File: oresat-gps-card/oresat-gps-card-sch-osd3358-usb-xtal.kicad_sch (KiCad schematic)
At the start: 42 parts, among them U1 OSD3358-512M-BSM, U11 RCLAMP0504FB, Y1 24MHz, Y2 Crystal

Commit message: Routine Push
Various small changes made
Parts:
- removed TP104, TP137, TP138, TP139, TP165, TP166, TP167, TP168, TP169, TP170, TP171, TP172, TP173, TP174, TP59, TP60, TP69, TP70, TP71, TP72: 0.03x0.04, oresat-misc:TestPoint_Pad_D1.0mm, symbol oresat-misc:Test-Point-1mm-round
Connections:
- no-connect marks 1 -> 15

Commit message: Routine Push
First attempt to clean up schematic
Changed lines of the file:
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@@
 		)
 	)
-	(global_label "USB_CLI_P"
+	(hierarchical_label "USB_CLI_N"
 		(shape input)
-		(at 119.38 198.12 180)
-		(fields_autoplaced yes)
+		(at 119.38 195.58 180)
 		(effects
 			(font
@@
 			(justify right)
 		)
-		(property "Intersheetrefs" "${INTERSHEET_REFS}"
-			(at 107.0488 198.0406 0)
-			(show_name no)
-			(do_not_autoplace no)
-			(effects
-				(font
-					(size 1.27 1.27)
-				)
-				(justify right)
-			)
-		)
 	)
-	(global_label "USB_CLI_N"
+	(hierarchical_label "nRESET"
 		(shape input)
-		(at 119.38 195.58 180)
-		(fields_autoplaced yes)
+		(at 147.32 200.66 180)
 		(effects
 			(font
@@
 			(justify right)
 		)
-		(property "Intersheetrefs" "${INTERSHEET_REFS}"
-			(at 106.9883 195.5006 0)
-			(show_name no)
-			(do_not_autoplace no)
-			(effects
-				(font
-					(size 1.27 1.27)
-				)
-				(justify right)
-			)
-		)
 	)
-	(global_label "USB_CLI_VBUS"
+	(hierarchical_label "USB_CLI_VBUS"
 		(shape input)
 		(at 119.38 193.04 180)
-		(fields_autoplaced yes)
 		(effects
 			(font
@@
 			(justify right)
 		)
-		(property "Intersheetrefs" "${INTERSHEET_REFS}"
-			(at 103.4202 192.9606 0)
-			(show_name no)
-			(do_not_autoplace no)
-			(effects
-				(font
-					(size 1.27 1.27)
-				)
-				(justify right)
-			)
-		)
 	)
-	(global_label "nRESET"
+	(hierarchical_label "VIN_USB"
 		(shape input)
-		(at 147.32 200.66 180)
-		(fields_autoplaced yes)
+		(at 137.16 177.8 180)
 		(effects
 			(font
@@
 			(justify right)
 		)
-		(property "Intersheetrefs" "${INTERSHEET_REFS}"
-			(at 137.5201 200.66 0)
-			(show_name no)
-			(do_not_autoplace no)
-			(effects
-				(font
-					(size 1.27 1.27)
-				)
-				(justify right)
-			)
-		)
 	)
-	(global_label "VIN_USB"
+	(hierarchical_label "USB_CLI_P"
 		(shape input)
-		(at 137.16 177.8 180)
-		(fields_autoplaced yes)
+		(at 119.38 198.12 180)
 		(effects
 			(font
@@
 			(justify right)
 		)
-		(property "Intersheetrefs" "${INTERSHEET_REFS}"
-			(at 126.9455 177.7206 0)
-			(show_name no)
-			(do_not_autoplace no)
-			(effects
-				(font
-					(size 1.27 1.27)
-				)
-				(justify right)
-			)
-		)
 	)

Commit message: Routine Push
Schematic finished. Components laid out, chasing ERCs.
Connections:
- no-connect marks 15 -> 16
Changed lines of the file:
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@@
+	)
+	(no_connect
+		(at 215.9 60.96)
 	)
 	(no_connect
@@
 		(pts
 			(xy 115.316 63.5) (xy 113.03 63.5)
-		)
-		(stroke
-			(width 0)
-			(type default)
-		)
-	)
-	(wire
-		(pts
-			(xy 215.9 60.96) (xy 218.44 60.96)
 		)
 		(stroke
@@
 			)
 		)
-		(property "Datasheet" ""
+		(property "Datasheet" "https://octavosystems.com/docs/osd335x-sm-datasheet/"
 			(at 185.42 106.68 0)
 			(hide yes)

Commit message: Routine Push
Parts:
- removed TP61, TP62, TP63, TP64, TP65, TP66, TP67: 0.03x0.04, oresat-misc:TestPoint_Pad_D1.0mm, symbol oresat-misc:Test-Point-1mm-round
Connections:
- no-connect marks 16 -> 23
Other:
- note added: "All resistors are 0603 1% AEC-Q200 unless marked. All capacitors are 0603 AEC-Q200 Vw >= 16V X5R or better unless marked."

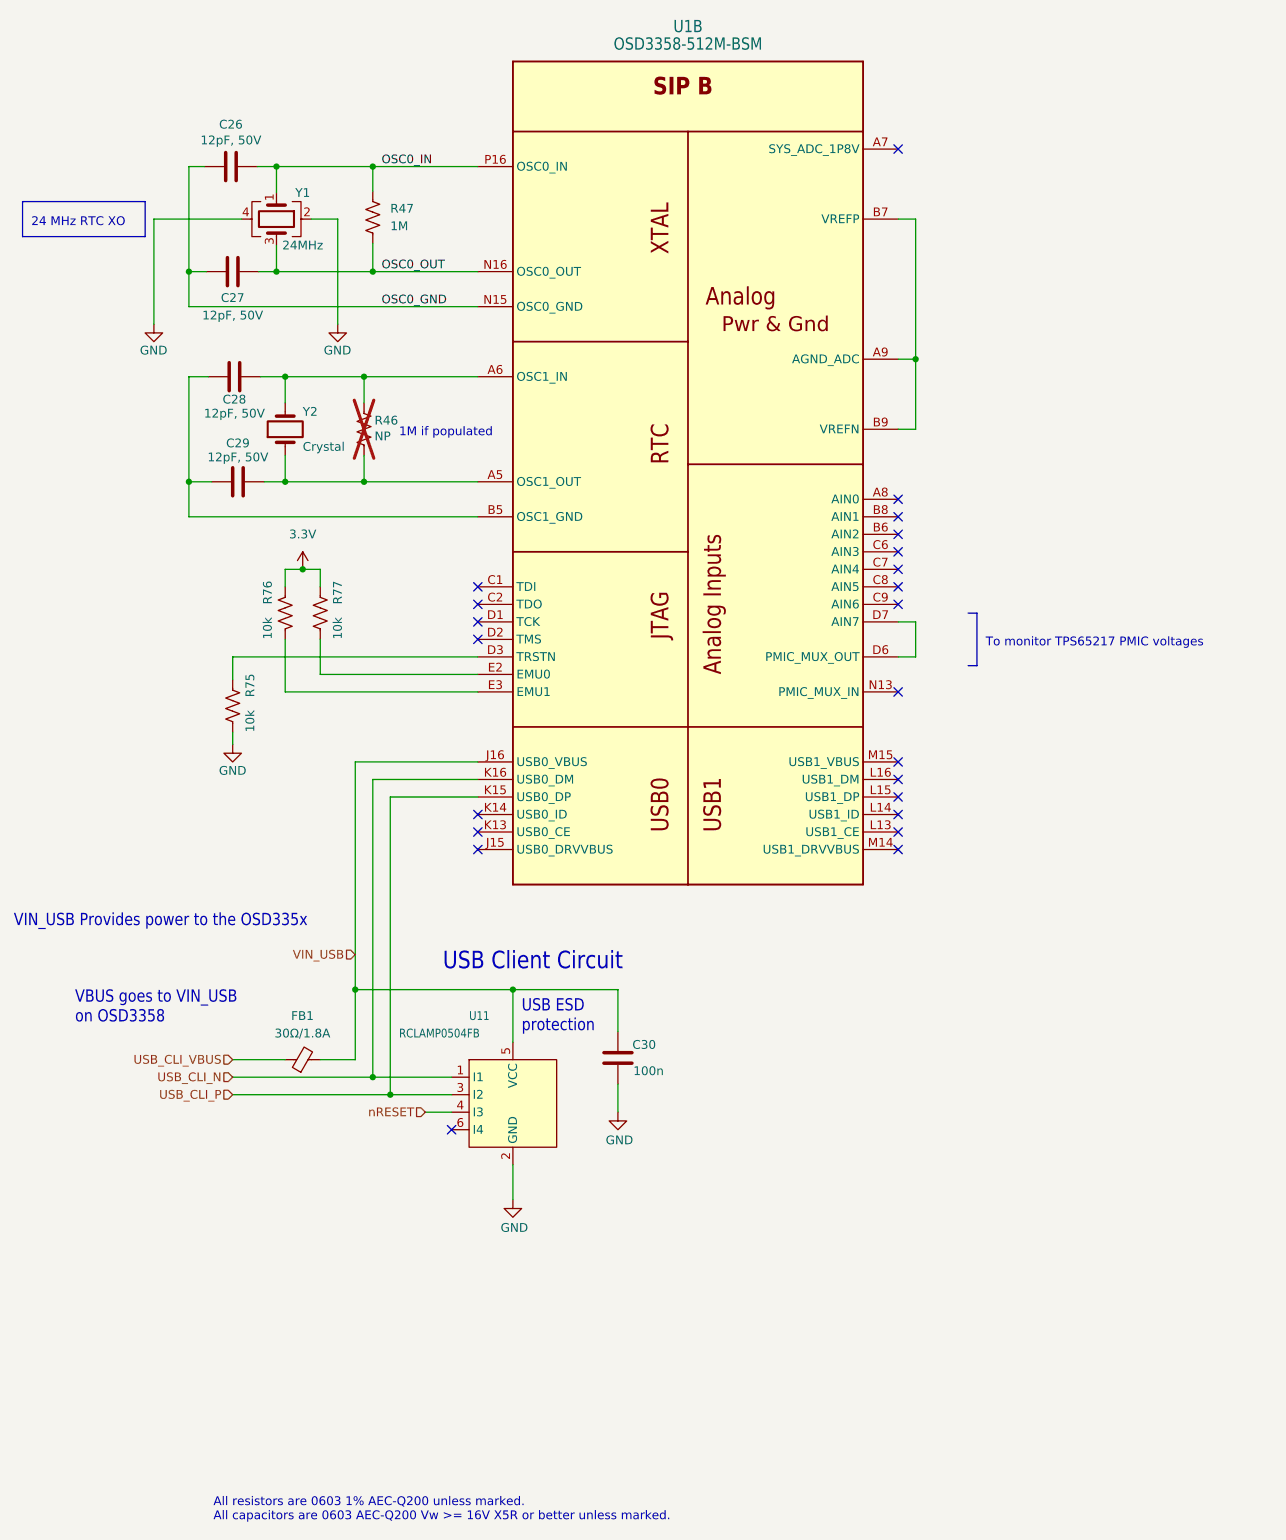
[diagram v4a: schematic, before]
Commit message: General cleanup of schematic and layout
Updated .gitignore, updates DRU file, moved RF lines to RF-50-MIN (max is just too big),
lots of cleanup on the root page to make it pretty, cleaned up some redudant labels,
updated SMPM connector and added rule zone, updated PCB outline to include NPTH drills
for SMPM connectors, began cleanup of OPD.
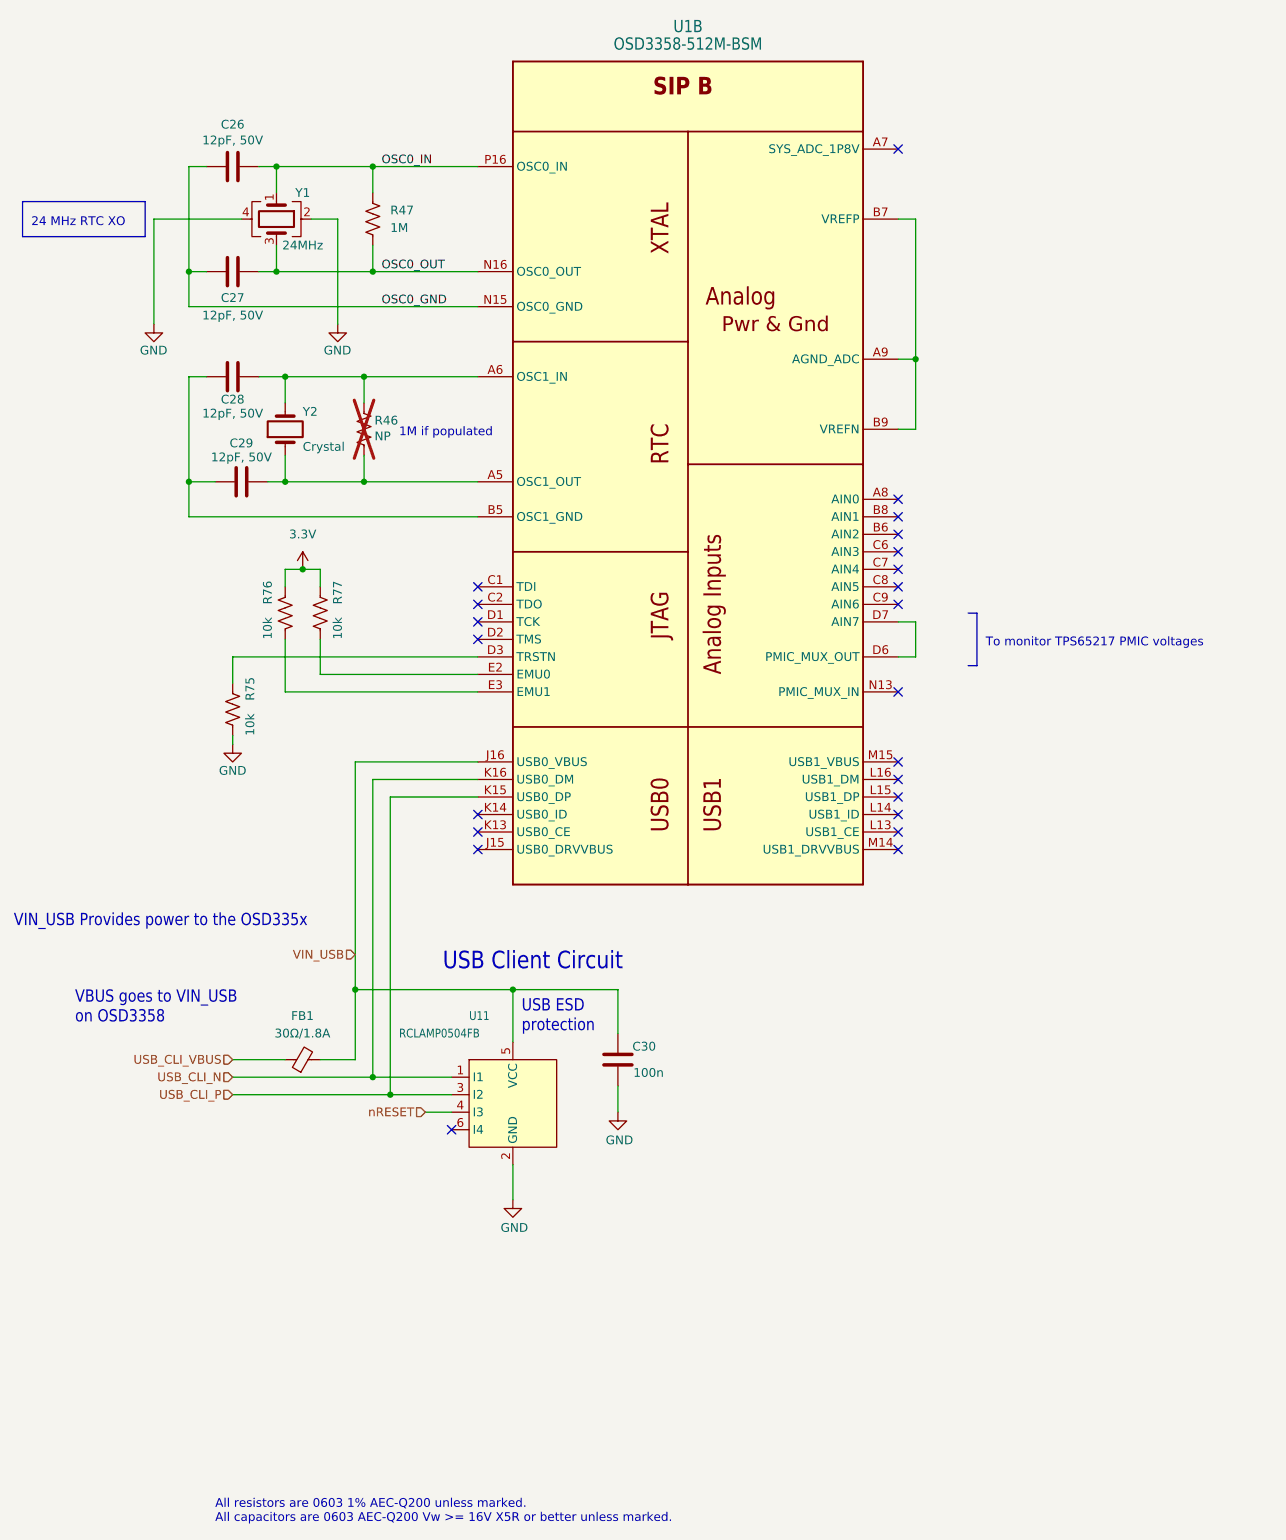
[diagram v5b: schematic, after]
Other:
- moved on the sheet: C29, R75
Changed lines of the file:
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@@
 	(text "All resistors are 0603 1% AEC-Q200 unless marked.\nAll capacitors are 0603 AEC-Q200 Vw >= 16V X5R or better unless marked."
 		(exclude_from_sim no)
-		(at 116.586 260.096 0)
+		(at 116.84 260.35 0)
 		(effects
 			(font
@@
 	(wire
 		(pts
-			(xy 175.26 182.88) (xy 175.26 188.976)
+			(xy 175.26 182.88) (xy 175.26 189.23)
 		)
 		(stroke
@@
 	(wire
 		(pts
-			(xy 119.38 145.542) (xy 119.38 147.32)
+			(xy 119.38 146.05) (xy 119.38 147.32)
 		)
 		(stroke
@@
 	(wire
 		(pts
-			(xy 127 109.22) (xy 123.952 109.22)
+			(xy 127 109.22) (xy 124.46 109.22)
 		)
 		(stroke
@@
 	(wire
 		(pts
-			(xy 116.332 109.22) (xy 113.03 109.22)
+			(xy 116.84 109.22) (xy 113.03 109.22)
 		)
 		(stroke
@@
 	(wire
 		(pts
-			(xy 139.7 74.676) (xy 139.7 78.74)
+			(xy 139.7 74.93) (xy 139.7 78.74)
 		)
 		(stroke
@@
 	(wire
 		(pts
-			(xy 119.38 134.62) (xy 119.38 137.922)
+			(xy 119.38 134.62) (xy 119.38 138.43)
 		)
 		(stroke
@@
 	(wire
 		(pts
-			(xy 115.316 63.5) (xy 113.03 63.5)
+			(xy 115.57 63.5) (xy 113.03 63.5)
 		)
 		(stroke
@@
 	(wire
 		(pts
-			(xy 139.7 63.5) (xy 139.7 67.056)
+			(xy 139.7 63.5) (xy 139.7 67.31)
 		)
 		(stroke
@@
 	(wire
 		(pts
-			(xy 123.444 93.98) (xy 127 93.98)
+			(xy 123.19 93.98) (xy 127 93.98)
 		)
 		(stroke
@@
 	(wire
 		(pts
-			(xy 113.03 93.98) (xy 115.824 93.98)
+			(xy 113.03 93.98) (xy 115.57 93.98)
 		)
 		(stroke
@@
 	(wire
 		(pts
-			(xy 175.26 196.596) (xy 175.26 200.66)
+			(xy 175.26 196.85) (xy 175.26 200.66)
 		)
 		(stroke
@@
 	(wire
 		(pts
-			(xy 122.936 63.5) (xy 125.73 63.5)
+			(xy 123.19 63.5) (xy 125.73 63.5)
 		)
 		(stroke
@@
 	(symbol
 		(lib_id "Device:C")
-		(at 175.26 192.786 180)
+		(at 175.26 193.04 180)
 		(unit 1)
 		(body_style 1)
@@
 		(dnp no)
 		(property "Reference" "C30"
-			(at 179.07 190.881 0)
+			(at 179.07 191.135 0)
 			(show_name no)
 			(do_not_autoplace no)
@@
 		)
 		(property "Value" "100n"
-			(at 179.705 194.691 0)
+			(at 179.705 194.945 0)
 			(show_name no)
 			(do_not_autoplace no)
@@
 		)
 		(property "Footprint" "Capacitor_SMD:C_0603_1608Metric"
-			(at 174.2948 188.976 0)
+			(at 174.2948 189.23 0)
 			(hide yes)
 			(show_name no)
@@
 		)
 		(property "Datasheet" ""
-			(at 175.26 192.786 0)
+			(at 175.26 193.04 0)
 			(hide yes)
 			(show_name no)
@@
 		)
 		(property "Description" "Unpolarized capacitor"
-			(at 175.26 192.786 0)
+			(at 175.26 193.04 0)
 			(hide yes)
 			(show_name no)
@@
 	(symbol
 		(lib_id "Device:C")
-		(at 120.142 109.22 90)
+		(at 120.65 109.22 90)
 		(unit 1)
 		(body_style 1)
@@
 		(dnp no)
 		(property "Reference" "C29"
-			(at 120.142 103.632 90)
+			(at 120.65 103.632 90)
 			(show_name no)
 			(do_not_autoplace no)
@@
 		)
 		(property "Value" "12pF, 50V"
-			(at 120.142 105.664 90)
+			(at 120.65 105.664 90)
 			(show_name no)
 			(do_not_autoplace no)
@@
 		)
 		(property "Footprint" "Capacitor_SMD:C_0603_1608Metric"
-			(at 123.952 108.2548 0)
+			(at 124.46 108.2548 0)
 			(hide yes)
 			(show_name no)
@@
 		)
 		(property "Datasheet" ""
-			(at 120.142 109.22 0)
+			(at 120.65 109.22 0)
 			(hide yes)
 			(show_name no)
@@
 		)
 		(property "Description" "Unpolarized capacitor"
-			(at 120.142 109.22 0)
+			(at 120.65 109.22 0)
 			(hide yes)
 			(show_name no)
@@
 	(symbol
 		(lib_id "Device:C")
-		(at 119.634 93.98 90)
+		(at 119.38 93.98 90)
 		(unit 1)
 		(body_style 1)
@@
 		(dnp no)
 		(property "Reference" "C28"
-			(at 119.634 97.282 90)
+			(at 119.38 97.282 90)
 			(show_name no)
 			(do_not_autoplace no)
@@
 		)
 		(property "Value" "12pF, 50V"
-			(at 119.634 99.314 90)
+			(at 119.38 99.314 90)
 			(show_name no)
 			(do_not_autoplace no)
@@
 		)
 		(property "Footprint" "Capacitor_SMD:C_0603_1608Metric"
-			(at 123.444 93.0148 0)
+			(at 123.19 93.0148 0)
 			(hide yes)
 			(show_name no)
@@
 		)
 		(property "Datasheet" ""
-			(at 119.634 93.98 0)
+			(at 119.38 93.98 0)
 			(hide yes)
 			(show_name no)
@@
 		)
 		(property "Description" "Unpolarized capacitor"
-			(at 119.634 93.98 0)
+			(at 119.38 93.98 0)
 			(hide yes)
 			(show_name no)
@@
 	(symbol
 		(lib_id "Device:C")
-		(at 119.126 63.5 90)
+		(at 119.38 63.5 90)
 		(unit 1)
 		(body_style 1)
@@
 		(dnp no)
 		(property "Reference" "C26"
-			(at 119.126 57.404 90)
+			(at 119.38 57.404 90)
 			(show_name no)
 			(do_not_autoplace no)
@@
 		)
 		(property "Value" "12pF, 50V"
-			(at 119.126 59.69 90)
+			(at 119.38 59.69 90)
 			(show_name no)
 			(do_not_autoplace no)
@@
 		)
 		(property "Footprint" "Capacitor_SMD:C_0603_1608Metric"
-			(at 122.936 62.5348 0)
+			(at 123.19 62.5348 0)
 			(hide yes)
 			(show_name no)
@@
 		)
 		(property "Datasheet" ""
-			(at 119.126 63.5 0)
+			(at 119.38 63.5 0)
 			(hide yes)
 			(show_name no)
@@
 		)
 		(property "Description" "Unpolarized capacitor"
-			(at 119.126 63.5 0)
+			(at 119.38 63.5 0)
 			(hide yes)
 			(show_name no)
@@
 	(symbol
 		(lib_id "Device:R_US")
-		(at 139.7 70.866 0)
+		(at 139.7 71.12 0)
 		(unit 1)
 		(body_style 1)
@@
 		(dnp no)
 		(property "Reference" "R47"
-			(at 142.24 69.5959 0)
+			(at 142.24 69.8499 0)
 			(show_name no)
 			(do_not_autoplace no)
@@
 		)
 		(property "Value" "1M"
-			(at 142.24 72.1359 0)
+			(at 142.24 72.3899 0)
 			(show_name no)
 			(do_not_autoplace no)
@@
 		)
 		(property "Footprint" "Resistor_SMD:R_0603_1608Metric"
-			(at 140.716 71.12 90)
+			(at 140.716 71.374 90)
 			(hide yes)
 			(show_name no)
@@
 		)
 		(property "Datasheet" ""
-			(at 139.7 70.866 0)
+			(at 139.7 71.12 0)
 			(hide yes)
 			(show_name no)
@@
 		)
 		(property "Description" "Resistor, US symbol"
-			(at 139.7 70.866 0)
+			(at 139.7 71.12 0)
 			(hide yes)
 			(show_name no)
@@
 	(symbol
 		(lib_id "Device:R_US")
-		(at 119.38 141.732 0)
+		(at 119.38 142.24 0)
 		(unit 1)
 		(body_style 1)
@@
 		(dnp no)
 		(property "Reference" "R75"
-			(at 121.92 140.462 90)
+			(at 121.92 140.97 90)
 			(show_name no)
 			(do_not_autoplace no)
@@
 		)
 		(property "Value" "10k"
-			(at 121.92 145.542 90)
+			(at 121.92 146.05 90)
 			(show_name no)
 			(do_not_autoplace no)
@@
 		)
 		(property "Footprint" "Resistor_SMD:R_0603_1608Metric"
-			(at 120.396 141.986 90)
+			(at 120.396 142.494 90)
 			(hide yes)
 			(show_name no)
@@
 		)
 		(property "Datasheet" ""
-			(at 119.38 141.732 0)
+			(at 119.38 142.24 0)
 			(hide yes)
 			(show_name no)
@@
 		)
 		(property "Description" "Resistor, US symbol"
-			(at 119.38 141.732 0)
+			(at 119.38 142.24 0)
 			(hide yes)
 			(show_name no)
